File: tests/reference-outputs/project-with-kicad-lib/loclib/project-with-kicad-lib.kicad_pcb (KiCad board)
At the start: 2 copper layers, 20.3 x 9.7 mm, 6 parts, among them U1 ADS1115IDGS

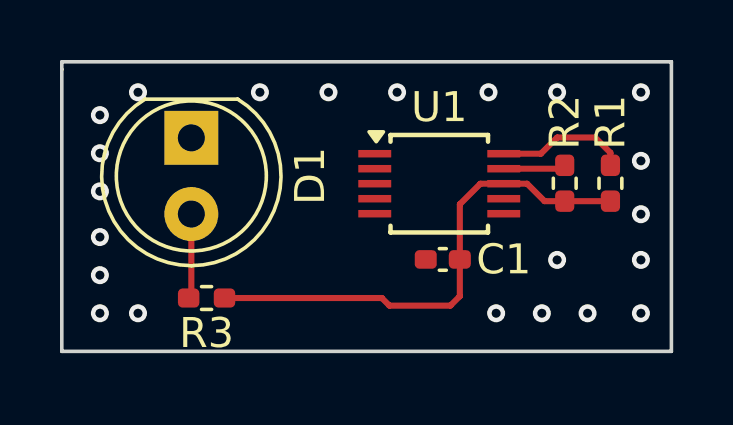
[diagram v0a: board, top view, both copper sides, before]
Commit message: [#63381] Add kibuzzard-to-graphic command
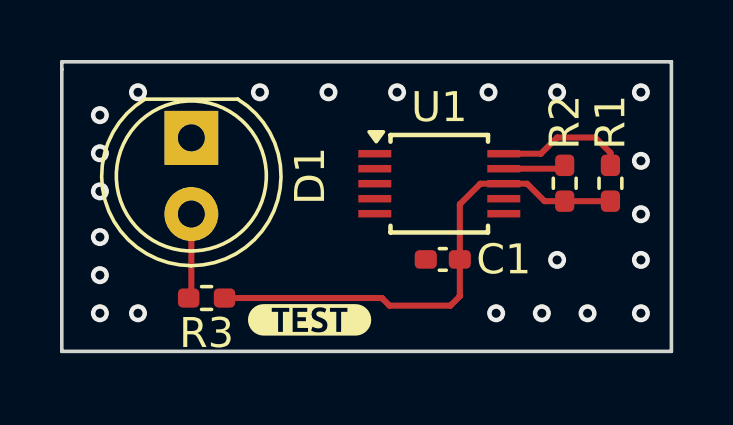
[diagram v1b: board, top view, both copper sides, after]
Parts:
- added kibuzzard-66D96414: G***, kibuzzard-66D96414, F.Cu at (137.8, 106.9)
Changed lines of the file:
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@@
     )
+  )
+  (footprint "kibuzzard-66D96414" (layer "F.Cu")
+    (at 137.8 106.9)
+    (descr "Generated with KiBuzzard")
+    (tags "kb_params=eyJBbGlnbm1lbnRDaG9pY2UiOiAiQ2VudGVyIiwgIkNhcExlZnRDaG9pY2UiOiAiKCIsICJDYXBSaWdodENob2ljZSI6ICIpIiwgIkZvbnRDb21ib0JveCI6ICJVYnVudHVNb25vLUIiLCAiSGVpZ2h0Q3RybCI6IDAuOCwgIkxheWVyQ29tYm9Cb3giOiAiRi5TaWxrUyIsICJMaW5lU3BhY2luZ0N0cmwiOiAxLjUsICJNdWx0aUxpbmVUZXh0IjogIlRFU1QiLCAiUGFkZGluZ0JvdHRvbUN0cmwiOiAxLjAsICJQYWRkaW5nTGVmdEN0cmwiOiAyLjUsICJQYWRkaW5nUmlnaHRDdHJsIjogMi41LCAiUGFkZGluZ1RvcEN0cmwiOiAxLjAsICJXaWR0aEN0cmwiOiAwLjAsICJhZHZhbmNlZENoZWNrYm94IjogdHJ1ZSwgImlubGluZUZvcm1hdFRleHRib3giOiBmYWxzZSwgImxpbmVvdmVyU3R5bGVDaG9pY2UiOiAiU3F1YXJlIiwgImxpbmVvdmVyVGhpY2tuZXNzQ3RybCI6IDF9")
+    (attr board_only exclude_from_pos_files exclude_from_bom)
+    (fp_text reference "kibuzzard-66D96414" (at 0 -3.573148) (layer "F.SilkS") hide
+      (effects (font (size 0 0)))
+    )
+    (fp_text value "G***" (at 0 3.573148) (layer "F.SilkS") hide
+      (effects (font (size 0 0)))
+    )
+    (fp_poly (pts
+        (xy -1.260097 -0.525148)
+        (xy -1.529348 -0.525148)
+        (xy -1.6318 -0.515058)
+        (xy -1.730314 -0.485174)
+        (xy -1.821105 -0.436645)
+        (xy -1.900684 -0.371336)
+        (xy -1.965993 -0.291757)
+        (xy -2.014522 -0.200965)
+        (xy -2.044406 -0.102451)
+        (xy -2.054496 0)
+        (xy -2.044406 0.102451)
+        (xy -2.014522 0.200965)
+        (xy -1.965993 0.291757)
+        (xy -1.900684 0.371336)
+        (xy -1.821105 0.436645)
+        (xy -1.730314 0.485174)
+        (xy -1.6318 0.515058)
+        (xy -1.529348 0.525148)
+        (xy -1.260097 0.525148)
+        (xy -0.889176 0.525148)
+        (xy -0.889176 0.400646)
+        (xy -1.049435 0.400646)
+        (xy -1.049435 -0.267528)
+        (xy -1.260097 -0.267528)
+        (xy -1.260097 -0.399354)
+        (xy -0.678514 -0.399354)
+        (xy -0.678514 -0.267528)
+        (xy -0.889176 -0.267528)
+        (xy -0.889176 0.400646)
+        (xy -0.889176 0.525148)
+        (xy -0.564782 0.525148)
+        (xy -0.564782 0.400646)
+        (xy -0.564782 -0.399354)
+        (xy -0.080129 -0.399354)
+        (xy -0.080129 -0.267528)
+        (xy -0.405816 -0.267528)
+        (xy -0.405816 -0.087884)
+        (xy -0.122779 -0.087884)
+        (xy -0.122779 0.043942)
+        (xy -0.405816 0.043942)
+        (xy -0.405816 0.268821)
+        (xy -0.051696 0.268821)
+        (xy -0.051696 0.400646)
+        (xy -0.564782 0.400646)
+        (xy -0.564782 0.525148)
+        (xy 0.299838 0.525148)
+        (xy 0.299838 0.417447)
+        (xy 0.210339 0.412116)
+        (xy 0.140872 0.396123)
+        (xy 0.051696 0.356704)
+        (xy 0.098223 0.227464)
+        (xy 0.181583 0.266236)
+        (xy 0.23538 0.279806)
+        (xy 0.299838 0.28433)
+        (xy 0.366397 0.275929)
+        (xy 0.408401 0.252666)
+        (xy 0.429725 0.219063)
+        (xy 0.435541 0.180937)
+        (xy 0.421325 0.136995)
+        (xy 0.385137 0.102746)
+        (xy 0.336026 0.075606)
+        (xy 0.281745 0.052989)
+        (xy 0.206785 0.023263)
+        (xy 0.136349 -0.019386)
+        (xy 0.084006 -0.08336)
+        (xy 0.063328 -0.178352)
+        (xy 0.081583 -0.278514)
+        (xy 0.136349 -0.35412)
+        (xy 0.191133 -0.389302)
+        (xy 0.258122 -0.410411)
+        (xy 0.337318 -0.417447)
+        (xy 0.4063 -0.413247)
+        (xy 0.465913 -0.400646)
+        (xy 0.55832 -0.363166)
+        (xy 0.511793 -0.240388)
+        (xy 0.440065 -0.271405)
+        (xy 0.34895 -0.28433)
+        (xy 0.278586 -0.274134)
+        (xy 0.236367 -0.243547)
+        (xy 0.222294 -0.192569)
+        (xy 0.235218 -0.151858)
+        (xy 0.268174 -0.12084)
+        (xy 0.313409 -0.096931)
+        (xy 0.363166 -0.077544)
+        (xy 0.441357 -0.04588)
+        (xy 0.516317 0.000646)
+        (xy 0.572536 0.073021)
+        (xy 0.589015 0.121971)
+        (xy 0.594507 0.182229)
+        (xy 0.576252 0.281906)
+        (xy 0.521486 0.356058)
+        (xy 0.464405 0.390163)
+        (xy 0.390522 0.410626)
+        (xy 0.299838 0.417447)
+        (xy 0.299838 0.525148)
+        (xy 1.049435 0.525148)
+        (xy 1.049435 0.400646)
+        (xy 0.889176 0.400646)
+        (xy 0.889176 -0.267528)
+        (xy 0.678514 -0.267528)
+        (xy 0.678514 -0.399354)
+        (xy 1.260097 -0.399354)
+        (xy 1.260097 -0.267528)
+        (xy 1.049435 -0.267528)
+        (xy 1.049435 0.400646)
+        (xy 1.049435 0.525148)
+        (xy 1.260097 0.525148)
+        (xy 1.529348 0.525148)
+        (xy 1.6318 0.515058)
+        (xy 1.730314 0.485174)
+        (xy 1.821105 0.436645)
+        (xy 1.900684 0.371336)
+        (xy 1.965993 0.291757)
+        (xy 2.014522 0.200965)
+        (xy 2.044406 0.102451)
+        (xy 2.054496 0)
+        (xy 2.044406 -0.102451)
+        (xy 2.014522 -0.200965)
+        (xy 1.965993 -0.291757)
+        (xy 1.900684 -0.371336)
+        (xy 1.821105 -0.436645)
+        (xy 1.730314 -0.485174)
+        (xy 1.6318 -0.515058)
+        (xy 1.529348 -0.525148)
+        (xy 1.260097 -0.525148)
+        (xy -1.260097 -0.525148)
+      ) (layer "F.SilkS") (stroke (width 0) (type solid)) (fill solid))
   )
   (footprint "project-with-kicad-lib-footprints:LED_D5.0mm" (layer "F.Cu")
